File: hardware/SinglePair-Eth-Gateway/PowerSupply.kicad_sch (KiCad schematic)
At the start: 17 parts, among them IC401 LDL112PV33R, J401 Wuerth-694108301002, U401 VXO7803-1000

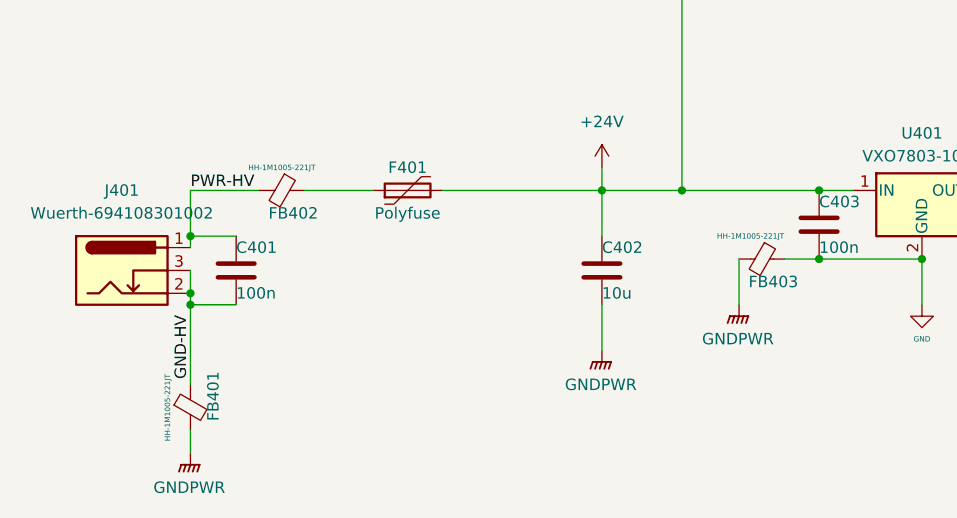
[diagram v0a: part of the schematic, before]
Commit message: Change position of values on the Fab layer
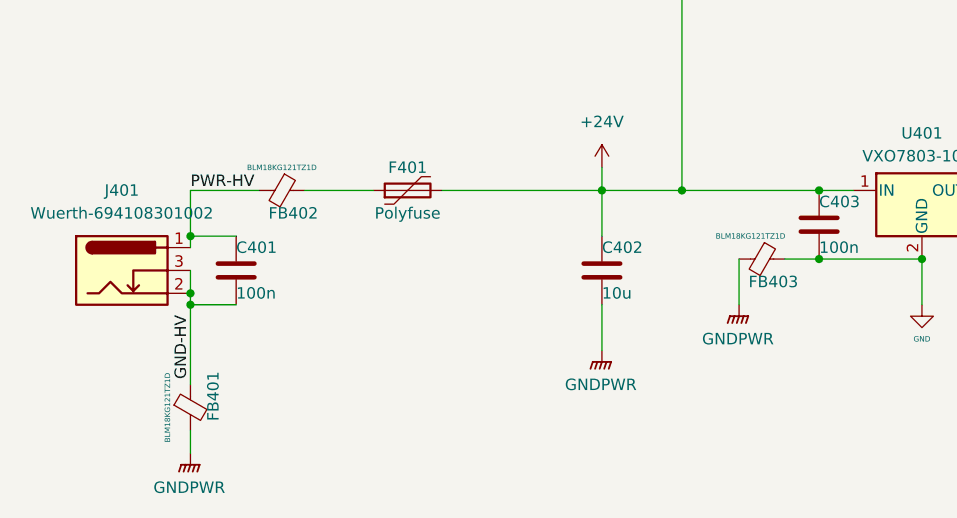
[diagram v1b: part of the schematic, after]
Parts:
- FB401, FB402, FB403: value HH-1M1005-221JT -> BLM18KG121TZ1D
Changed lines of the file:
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@@
       (effects (font (size 1.27 1.27)))
     )
-    (property "Value" "HH-1M1005-221JT" (at 50.8 146.05 90)
+    (property "Value" "BLM18KG121TZ1D" (at 50.8 146.05 90)
       (effects (font (size 0.6 0.6)))
     )
@@
       (effects (font (size 1.27 1.27)))
     )
-    (property "Value" "HH-1M1005-221JT" (at 63.5 119.38 90)
+    (property "Value" "BLM18KG121TZ1D" (at 63.5 119.38 90)
       (effects (font (size 0.6 0.6)))
     )
@@
       (effects (font (size 1.27 1.27)))
     )
-    (property "Value" "HH-1M1005-221JT" (at 115.57 127 90)
+    (property "Value" "BLM18KG121TZ1D" (at 115.57 127 90)
       (effects (font (size 0.6 0.6)))
     )
